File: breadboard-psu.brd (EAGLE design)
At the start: 38.1 x 53.3 mm, 23 parts, among them J1 DC_IN, J2 5V-BOARD, J3 5V-CABLE, J4 3.3V-BOARD, J5 3.3V-CABLE, K1 POWER, K2 5V, K3 3.3V, U1 AP1117T50G-U, U2 AP1117T33G-U

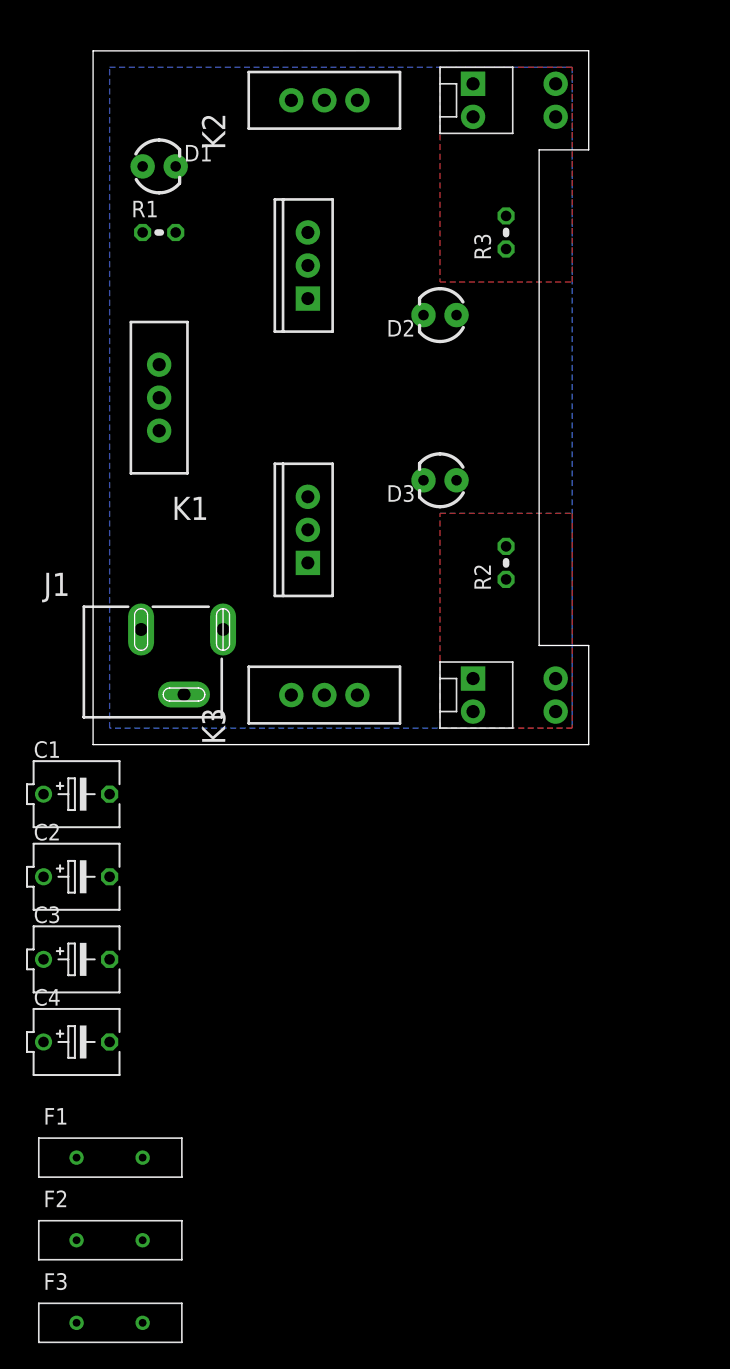
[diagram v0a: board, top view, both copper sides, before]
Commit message: UPDATE:  - first draft, schematic is stable, layout is routed and poured.  - still left to do the silkscreen and confirm width (to match breadboard).  - all footprints checked or generated in-situ to match the actual BOM.
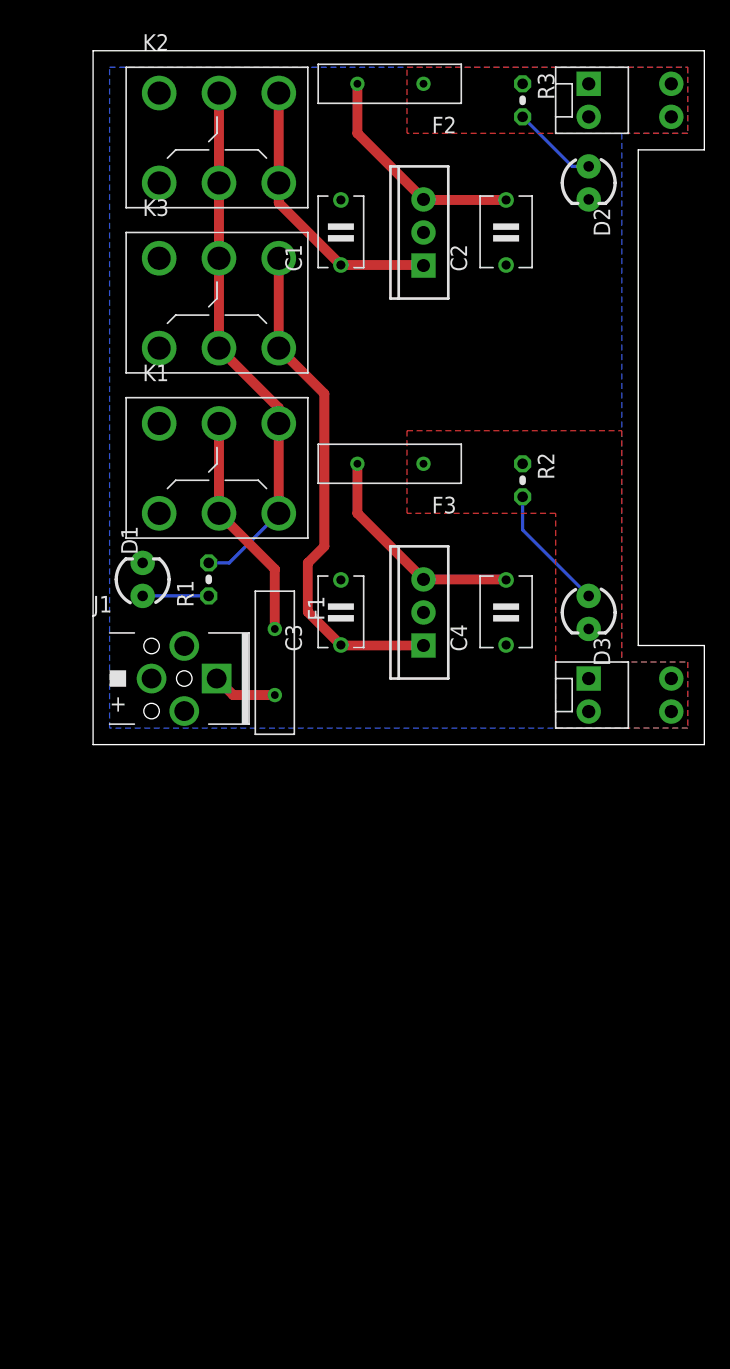
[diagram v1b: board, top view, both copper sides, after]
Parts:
- C1: device rcl:ETR3 -> radu-collected:FK26*
- C2, C4: value 22uF, 6.3V -> 22uF, 10V; device rcl:ETR3 -> radu-collected:FK20*
- C3: value 10uF, 16V -> 10uF, 16v; device rcl:ETR3 -> radu-collected:FK26*
- J1: value DC_IN -> 163-5010-E; device SparkFun-Connectors:POWER_JACK_SLOT -> radu-collected:163-501*-E
- K1: value POWER -> GF-126-0159; device SparkFun-Electromechanical:SWITCH-SPDT -> radu-collected:GF-126-0159
- K2: value 5V -> GF-126-0159; device SparkFun-Electromechanical:SWITCH-SPDT -> radu-collected:GF-126-0159
- K3: value 3.3V -> GF-126-0159; device SparkFun-Electromechanical:SWITCH-SPDT -> radu-collected:GF-126-0159
- moved F2 91.5 mm to (22.9, 50.8), turned to 180 degrees
- moved F3 69.5 mm to (22.9, 21.6), turned to 180 degrees
- moved C2 59.5 mm to (31.8, 39.4), turned to 90 degrees
- moved C1 47.7 mm to (19.1, 39.4), turned to 90 degrees
- moved C4 46.7 mm to (31.8, 10.2), turned to 90 degrees
- moved F1 40.2 mm to (14.0, 6.35), turned to 270 degrees
- moved C3 33.5 mm to (19.1, 10.2), turned to 90 degrees
- moved D1 31.8 mm to (3.81, 12.7), turned to 90 degrees
- moved K3 29.5 mm to (5.08, 30.5), turned to 0 degrees
- moved R1 26.9 mm to (8.89, 12.7), turned to 90 degrees
- moved D3 15.3 mm to (38.1, 10.2), turned to 270 degrees
- moved D2 15.3 mm to (38.1, 43.2), turned to 270 degrees
- moved K2 14.2 mm to (5.08, 43.2), turned to 0 degrees
- moved U2 10.9 mm to (25.4, 10.2)
- moved R3 10.2 mm to (33.0, 49.5), turned to 270 degrees
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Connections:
- net 3V3: no longer C4.+
- net 5V: now also R3.1; no longer C2.+, R3.2
- net GND: now also C1.P$2, C2.P$1, C3.P$2, C4.P$1, J1.P$1; no longer C1.-, C2.-, C3.-, C4.-, J1.GND@2
- net N$1: now also J1.P$4; no longer J1.PWR
- net N$10: now also R3.2; no longer R3.1
- net N$2: now also K1.P$2, K1.P$5; no longer K1.2
- net N$3: now also K1.P$3, K1.P$6, K2.P$2, K2.P$5, K3.P$2, K3.P$5; no longer K1.3, K2.2, K3.2
- net N$4: now also C1.P$1, K2.P$3, K2.P$6; no longer C1.+, K2.3
- net N$5: now also C3.P$1, K3.P$3, K3.P$6; no longer C3.+, K3.3
- net N$6: now also C2.P$2
- net N$7: now also C4.P$2
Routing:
- net N$3: track 0.00 -> 41.2 mm
- net N$5: track 0.00 -> 39.1 mm
- net N$4: track 0.00 -> 21.6 mm
- net N$2: track 0.00 -> 17.6 mm
- net N$7: track 0.00 -> 17.4 mm
- net N$6: track 0.00 -> 17.4 mm
- net N$13: track 0.00 -> 9.72 mm
- net N$10: track 0.00 -> 6.66 mm
- net N$9: track 0.00 -> 5.08 mm
- net N$1: track 0.00 -> 5.00 mm
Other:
- board size 38.1 x 53.3 mm -> 47 x 53.3 mm

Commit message: UPDATE:  - redesigned without fangs as various breadboards have various widths, leaving just cable version in  - this allows us to fit in 5x5cm with drastic reduction in price
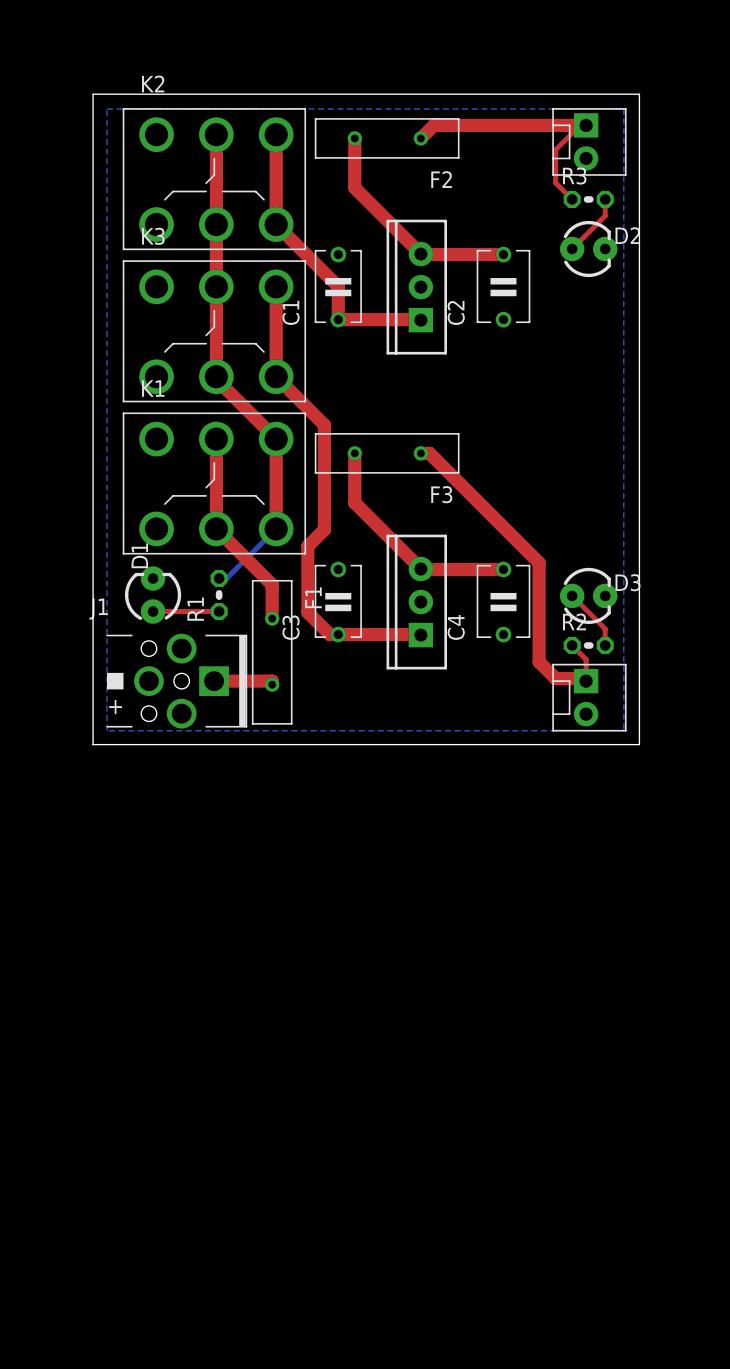
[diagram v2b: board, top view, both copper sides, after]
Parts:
- removed J2: 5V-BOARD, SparkFun-Connectors:1X02
- removed J4: 3.3V-BOARD, SparkFun-Connectors:1X02
- moved R2 13.7 mm to (38.1, 7.62), turned to 0 degrees
- moved R3 9.16 mm to (38.1, 41.9), turned to 0 degrees
- moved D2 5.08 mm to (38.1, 38.1), turned to 0 degrees
- moved C1 4.20 mm to (18.9, 35.2)
- moved C2 4.20 mm to (31.6, 35.2)
- moved F2 4.20 mm to (22.7, 46.6)
- moved U1 4.20 mm to (25.2, 35.2)
- moved K2 3.21 mm to (4.88, 40.0)
- moved J3 3.21 mm to (37.9, 47.6)
- moved K3 2.21 mm to (4.88, 28.3)
- moved D1 1.44 mm to (4.61, 11.5)
- moved R1 1.44 mm to (9.69, 11.5)
- moved D3 1.27 mm to (38.1, 11.4), turned to 0 degrees
- moved K1 1.22 mm to (4.88, 16.6)
- moved F1 0.82 mm to (13.8, 7.15)
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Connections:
- net 3V3: no longer J4.1
- net 5V: no longer J2.1
- net GND: no longer J2.2, J4.2
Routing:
- net 3V3: track 0.00 -> 27.6 mm
- net 5V: track 0.00 -> 20.6 mm
- net N$13: track 9.72 -> 4.86 mm
- net N$3: track 41.2 -> 38.2 mm
- net N$5: track 39.1 -> 36.5 mm
- net N$2: track 17.6 -> 15.6 mm
- net N$10: track 6.66 -> 4.86 mm
- net N$4: track 21.6 -> 22.6 mm
- removed copper zone on layer 1, net 3V3
- removed copper zone on layer 1, net 5V
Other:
- board size 47 x 53.3 mm -> 42 x 50 mm

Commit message: UPDATE:  - PCB done, including silk, aesthetics, physicals and design for manufacturing  - this is ready to go to the fab.
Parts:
- added LOGO2: OSHW-LOGOL, SparkFun-Aesthetics:OSHW-LOGO-L
- D1, D2, D3: device SparkFun-LED:LED3MM -> led:LED3MM
- moved D1 0.18 mm to (4.45, 11.4)
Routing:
- net 5V: track 20.6 -> 19.3 mm
- net 3V3: track 27.6 -> 27.0 mm
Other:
- board text added: "+"
- board text added: "-"
- board text added: "20150224"
- board text added: "3.3V"
- board text added: "5V"
- board text added: "Author: Radu - Eosif Mihailescu"
- board text added: "BB-PSU for Makers-IE"
- board text added: "BOTC"
- board text added: "BOTS"
- board text added: "POWER"
- board text added: "TOPC"
- board text added: "TOPS"
- board text added: "https://github.com/csdexter/breadboard-psu"
